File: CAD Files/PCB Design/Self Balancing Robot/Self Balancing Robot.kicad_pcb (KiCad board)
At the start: 2 copper layers, 87.4 x 52.6 mm, 22 parts, among them J1 XT60 Female, M1 Stepper_Motor_bipolar, M2 Stepper_Motor_bipolar, U1 DEVKIT_V1_ESP32-WROOM-32, U2 TSR_1-2450

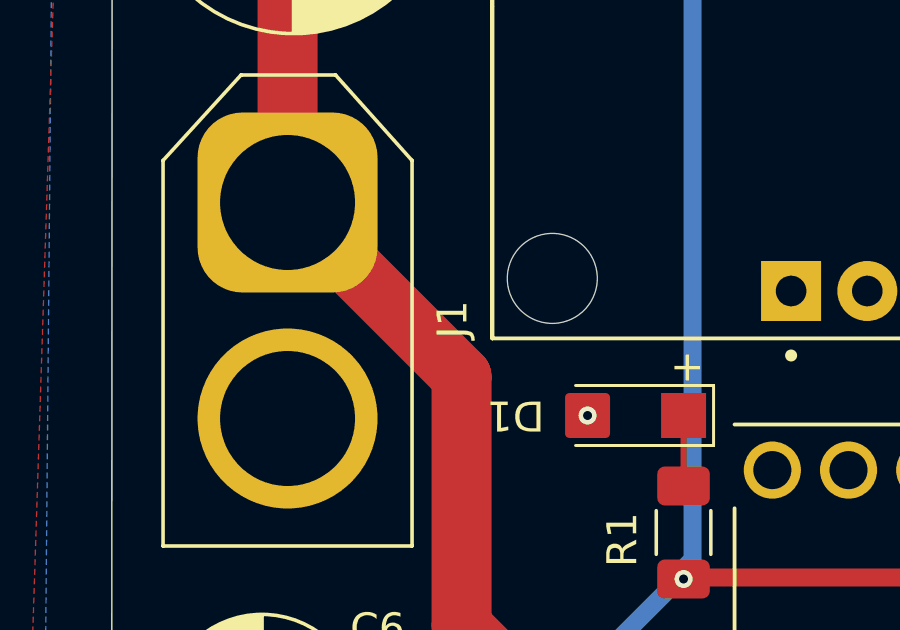
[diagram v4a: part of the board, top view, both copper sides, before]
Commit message: Replace XT60 Female with Male header
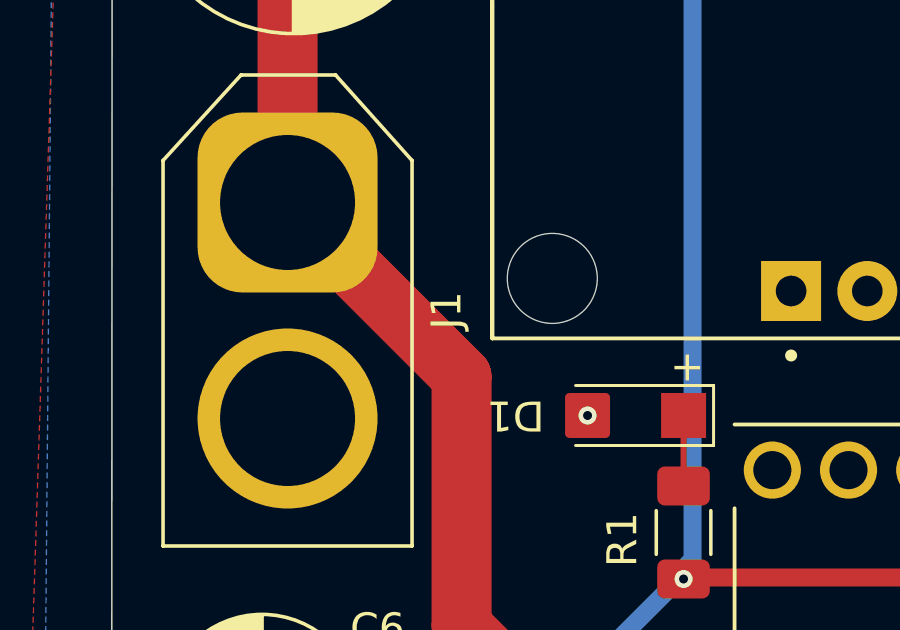
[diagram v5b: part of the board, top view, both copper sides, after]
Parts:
- J1: value XT60 Female -> XT60 Male; footprint Connector_AMASS:AMASS_XT60-F_1x02_P7.20mm_Vertical -> Connector_AMASS:AMASS_XT60-M_1x02_P7.20mm_Vertical
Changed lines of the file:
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@@
 		)
 	)
-	(footprint "Connector_AMASS:AMASS_XT60-F_1x02_P7.20mm_Vertical"
+	(footprint "Connector_AMASS:AMASS_XT60-M_1x02_P7.20mm_Vertical"
 		(layer "F.Cu")
 		(at 92.2 65 -90)
@@
 		(tags "XT60 female vertical")
 		(property "Reference" "J1"
-			(at 3.9 -5.5 90)
+			(at 3.6 -5.3 90)
 			(layer "F.SilkS")
 			(effects
@@
 			)
 		)
-		(property "Value" "XT60 Female"
-			(at 3.6 5.4 90)
+		(property "Value" "XT60 Male"
+			(at 3.6 5.4 270)
 			(layer "F.Fab")
 			(effects
@@
 		)
 		(fp_text user "${REFERENCE}"
-			(at 3.6 0.05 90)
+			(at 3.6 0.05 270)
 			(layer "F.Fab")
 			(effects
@@
 		)
 		(embedded_fonts no)
-		(model "${KICAD9_3DMODEL_DIR}/Connector_AMASS.3dshapes/AMASS_XT60-F_1x02_P7.2mm_Vertical.step"
+		(model "${KICAD9_3DMODEL_DIR}/Connector_AMASS.3dshapes/AMASS_XT60-M_1x02_P7.2mm_Vertical.step"
 			(offset
 				(xyz 0 0 0)

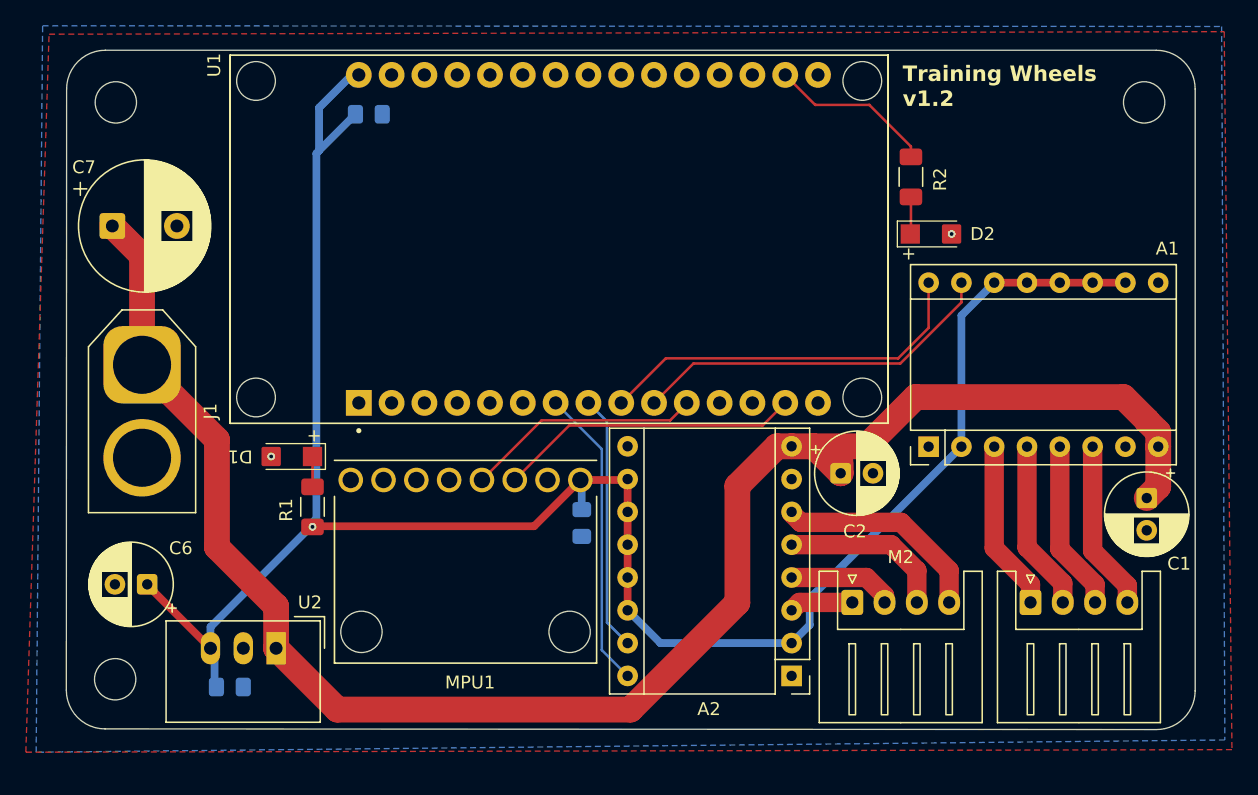
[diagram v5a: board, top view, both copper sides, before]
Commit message: Flip VCC cap to top, laid ground traces as suggested by Dr. Roan
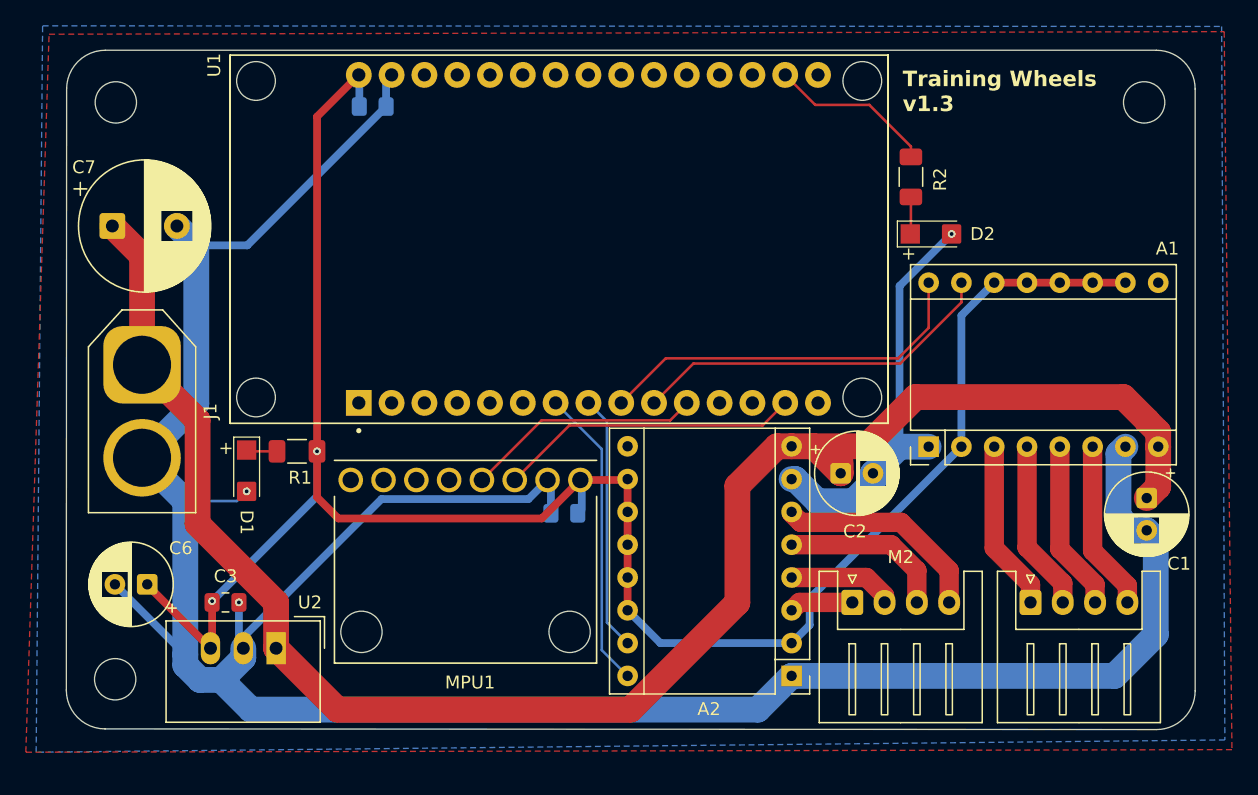
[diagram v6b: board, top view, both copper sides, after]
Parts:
- C3: moved to F.Cu
- moved C3 6.56 mm to (98.7, 83.4)
- moved R1 4.46 mm to (104.2, 71.7), turned to 180 degrees
- moved D1 3.67 mm to (100.3, 73.2), turned to -90 degrees
- moved C5 1.54 mm to (124.9, 76.5), turned to 180 degrees
- moved C4 0.67 mm to (110.1, 45.0)
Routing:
- net GND: track 0.00 -> 238.5 mm, vias 2 -> 3
- net VDD: track 160.8 -> 160.4 mm, vias 1 -> 2
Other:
- board text added: "Training Wheels v1.3"
- board text removed: "Training Wheels v1.2"

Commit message: Fix edge cuts to generate .step
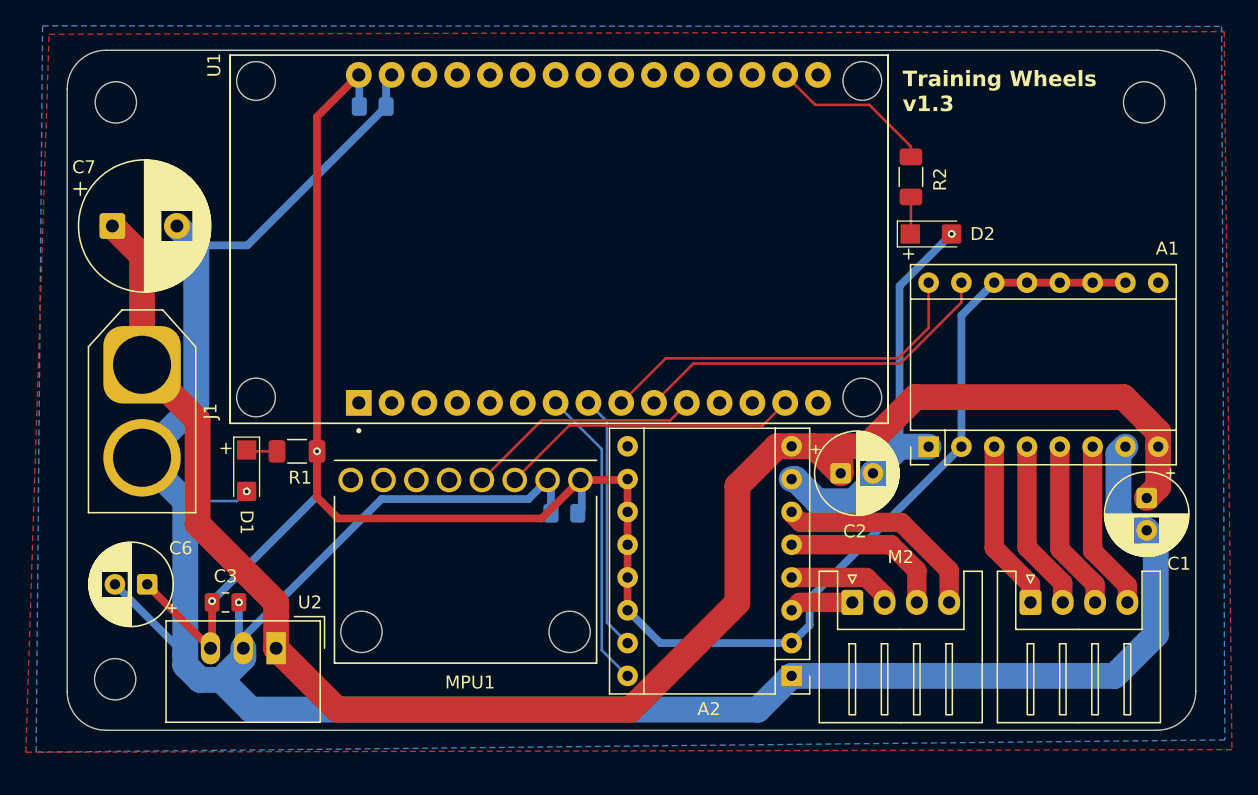
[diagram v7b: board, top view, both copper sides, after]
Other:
- board size 87.4 x 52.6 mm -> 87.4 x 52.7 mm
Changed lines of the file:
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@@
 			(drillshape 0)
 			(scaleselection 1)
-			(outputdirectory "./")
+			(outputdirectory "Actual Geber Files/")
 		)
 	)
@@
 	)
 	(gr_line
-		(start 173.75 43.644652)
-		(end 173.75 90.2462)
+		(start 86.4 90.3)
+		(end 86.4 43.64)
 		(stroke
 			(width 0.05)
@@
 	)
 	(gr_arc
-		(start 173.75 90.2462)
-		(mid 172.870666 92.368175)
-		(end 170.748149 93.2462)
+		(start 173.8 90.3)
+		(mid 172.92132 92.42132)
+		(end 170.8 93.3)
 		(stroke
 			(width 0.05)
@@
 	)
 	(gr_arc
-		(start 89.334198 93.194451)
-		(mid 87.213562 92.314604)
-		(end 86.33605 90.193002)
+		(start 86.4 43.64)
+		(mid 87.27868 41.51868)
+		(end 89.4 40.64)
 		(stroke
 			(width 0.05)
@@
 	)
 	(gr_line
-		(start 89.35855 40.64)
-		(end 170.75 40.64)
+		(start 89.4 40.64)
+		(end 170.8 40.64)
 		(stroke
 			(width 0.05)
@@
 	)
 	(gr_arc
-		(start 170.75 40.644652)
-		(mid 172.871337 41.523329)
-		(end 173.75 43.644652)
+		(start 89.4 93.3)
+		(mid 87.27868 92.42132)
+		(end 86.4 90.3)
 		(stroke
 			(width 0.05)
@@
 	)
 	(gr_line
-		(start 170.748149 93.2462)
-		(end 89.334198 93.194451)
+		(start 170.8 93.3)
+		(end 89.4 93.3)
 		(stroke
 			(width 0.05)
@@
 	)
 	(gr_arc
-		(start 86.358551 43.63855)
-		(mid 87.237743 41.518168)
-		(end 89.35855 40.64)
+		(start 170.8 40.64)
+		(mid 172.92132 41.51868)
+		(end 173.8 43.64)
 		(stroke
 			(width 0.05)
@@
 	)
 	(gr_line
-		(start 86.33605 90.193002)
-		(end 86.358551 43.63855)
+		(start 173.8 43.64)
+		(end 173.8 90.3)
 		(stroke
 			(width 0.05)
